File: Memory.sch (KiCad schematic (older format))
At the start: 60 parts, among them Q401 2N2222, Q402 2N2222, U401 74HCT74N, U402 74HCT08N, U403 74HCT08N, U404 74LS04, U406 74HCT08N, U407 74HCT138N, U408 74HCT74N, U409 74HCT273N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

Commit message: Pre-removal of H/L byte deciding hardware
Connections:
- net labels added: MARH_IN, MARL_IN
- net labels removed: MAR_IN
- wire segments 392 -> 390
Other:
- note added: "Initial state: 0b0\nAfter MAR_IN rises 1x: 0b1 (ready to read in low byte)\nAfter MAR_IN rises 2x: 0b0 (ready to read in high byte)\nAt 3x, this tff has cycled to the first MAR_IN rising condition\n"
- note removed: "Initial state: 0b0\nAfter MAR_IN rises 1x: 0b1 (ready to read in high byte)\nAfter MAR_IN rises 2x: 0b0 (ready to read in low byte)\nAt 3x, this tff has cycled to the first MAR_IN rising condition\n"
- moved on the sheet: C402, C403, C404, C405, C406, C407, C408, C409, C410, C411, C412, C413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

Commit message: Testing memory module
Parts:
- removed C404, C409: 0.1u, symbol Breadboard_CPU-rescue:C_Small-Device
- removed Q402: 2N2222, symbol Breadboard_CPU-rescue:Q_NPN_CBE-Device
- removed R402: 4.7k, symbol Breadboard_CPU-rescue:R-Device
- removed R405: 10k, symbol Breadboard_CPU-rescue:R-Device
- removed U401: 74HCT74N, symbol Breadboard_CPU-rescue:74LS74-74xx
- removed unit 3 of U402
- removed unit 4 of U402
- removed unit 1 of U403
- removed unit 2 of U406
- removed unit 3 of U406
- removed unit 5 of U406
- removed unit 1 of U408
- removed unit 2 of U408
- removed U411, U414: 74HCT32N, symbol Breadboard_CPU-rescue:74LS32-74xx
- removed U413: AS6C6264, symbol Memory:AS6C6264
- added unit 3 of U403
- added U650: 74HCT74N, symbol Breadboard_CPU-rescue:74LS74-74xx
- added U? (x5): 74HCT32, symbol 74xx:74LS32
- added U?: AS6C6264-55PCN, symbol Memory:AS6C6264-55PCN
- C410: value 0.1n -> 0.1u
- R401: value 4.7k -> 100
- R403: value 10k -> 270
- R404: value 10k -> 1k
- renumbered U406 to U402, U403 to U402, U406 to U403
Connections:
- net labels added: MEM_RD_HB
- net labels removed: CLK_MAR_IN, ~CLK
- wire segments 390 -> 339
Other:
- note added: "EEPROM for user and OS code\n(2048 instructions)"
- note added: "For ~CE~ to be active (low):\n- MAR[15] must be active (high)\n- PB_SEL must be inactive (low)"
- note added: "For ~CE~ to be active (low):\n- MAR[15] must be inactive (low)"
- note added: "SRAM for runtime memory\n(8KB)"
- note removed: "EEPROM for user\nand OS code"
- note removed: "Initial state: 0b0\nAfter MAR_IN rises 1x: 0b1 (ready to read in low byte)\nAfter MAR_IN rises 2x: 0b0 (ready to read in high byte)\nAt 3x, this tff has cycled to the first MAR_IN rising condition\n"
- note removed: "SRAM for active use (16 KB available)"
- note removed: "When MEM_OUT and MAR[15] go low, we are accessing the code EEPROM\nToggle the"
- moved on the sheet: C403, C408, U402A, U402B, U402C, U402D, U403A, U403B, U403D, U404A, U404B, U404C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

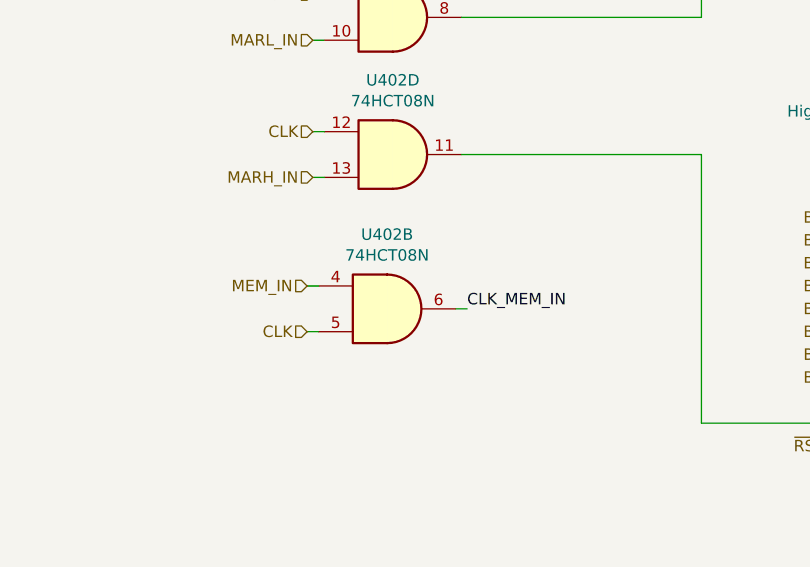
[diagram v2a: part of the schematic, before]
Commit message: Simulating negpulse
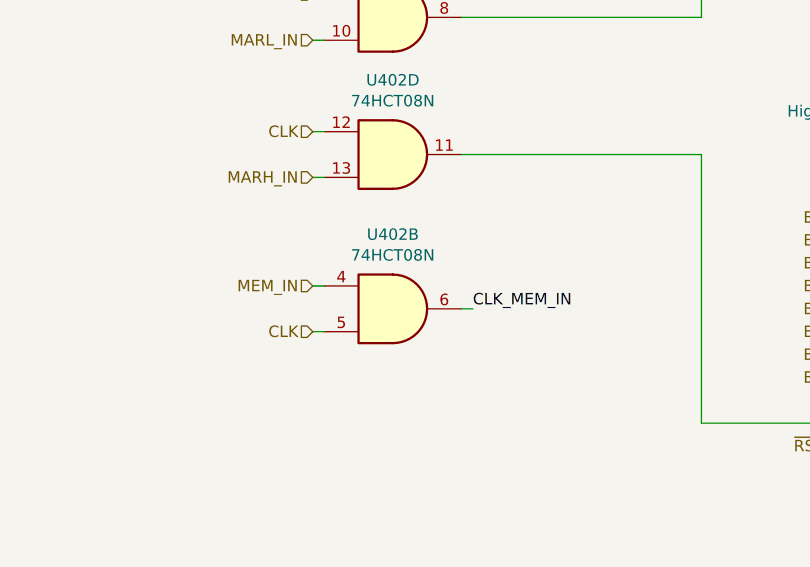
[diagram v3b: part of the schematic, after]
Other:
- moved on the sheet: U402B
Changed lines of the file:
@@
 Wire Wire Line
 	13175 3650 13225 3650
-Text HLabel 4475 4250 0    50   Input ~ 0
+Text HLabel 4500 4250 0    50   Input ~ 0
 CLK
 Wire Wire Line
-	4525 4250 4475 4250
-Text HLabel 4475 4050 0    50   Input ~ 0
+	4550 4250 4500 4250
+Text HLabel 4500 4050 0    50   Input ~ 0
 MEM_IN
 Wire Wire Line
-	4475 4050 4525 4050
+	4500 4050 4550 4050
 $Comp
 L Breadboard_CPU-rescue:C_Small-Device C408
@@
 L Breadboard_CPU-rescue:74LS08-74xx U?
 U 2 1 61B90A7D
-P 4825 4150
+P 4850 4150
 AR Path="/5EFC06D4/61B90A7D" Ref="U?"  Part="2"
 AR Path="/5EFC0623/61B90A7D" Ref="U402"  Part="2"
-F 0 "U402" H 4825 4475 50  0000 C CNN
-F 1 "74HCT08N" H 4825 4384 50  0000 C CNN
-F 2 "" H 4825 4150 50  0001 C CNN
-F 3 "http://www.ti.com/lit/gpn/sn74LS08" H 4825 4150 50  0001 C CNN
-	2    4825 4150
+F 0 "U402" H 4850 4475 50  0000 C CNN
+F 1 "74HCT08N" H 4850 4384 50  0000 C CNN
+F 2 "" H 4850 4150 50  0001 C CNN
+F 3 "http://www.ti.com/lit/gpn/sn74LS08" H 4850 4150 50  0001 C CNN
+	2    4850 4150
 	1    0    0    -1
 $EndComp
@@
 	4175 6150 5450 6150
 Wire Wire Line
-	5125 4150 5175 4150
-Text Label 5175 4150 0    50   ~ 0
+	5150 4150 5200 4150
+Text Label 5200 4150 0    50   ~ 0
 CLK_MEM_IN
 Text Label 13625 3650 0    50   ~ 0
